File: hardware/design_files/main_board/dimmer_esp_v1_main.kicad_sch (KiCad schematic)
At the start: 53 parts, among them IC1 PEC11S-929K-S0015, J1 SM05B-SRSS-TB_LF__SN_, J4 Conn_01x02, J5 Conn_01x02, J6 Conn_01x02, J7 Conn_01x04, J8 Screw_Terminal_01x03, K1 FTR-LYCA005Y, SW1 Commission, SW2 Reset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

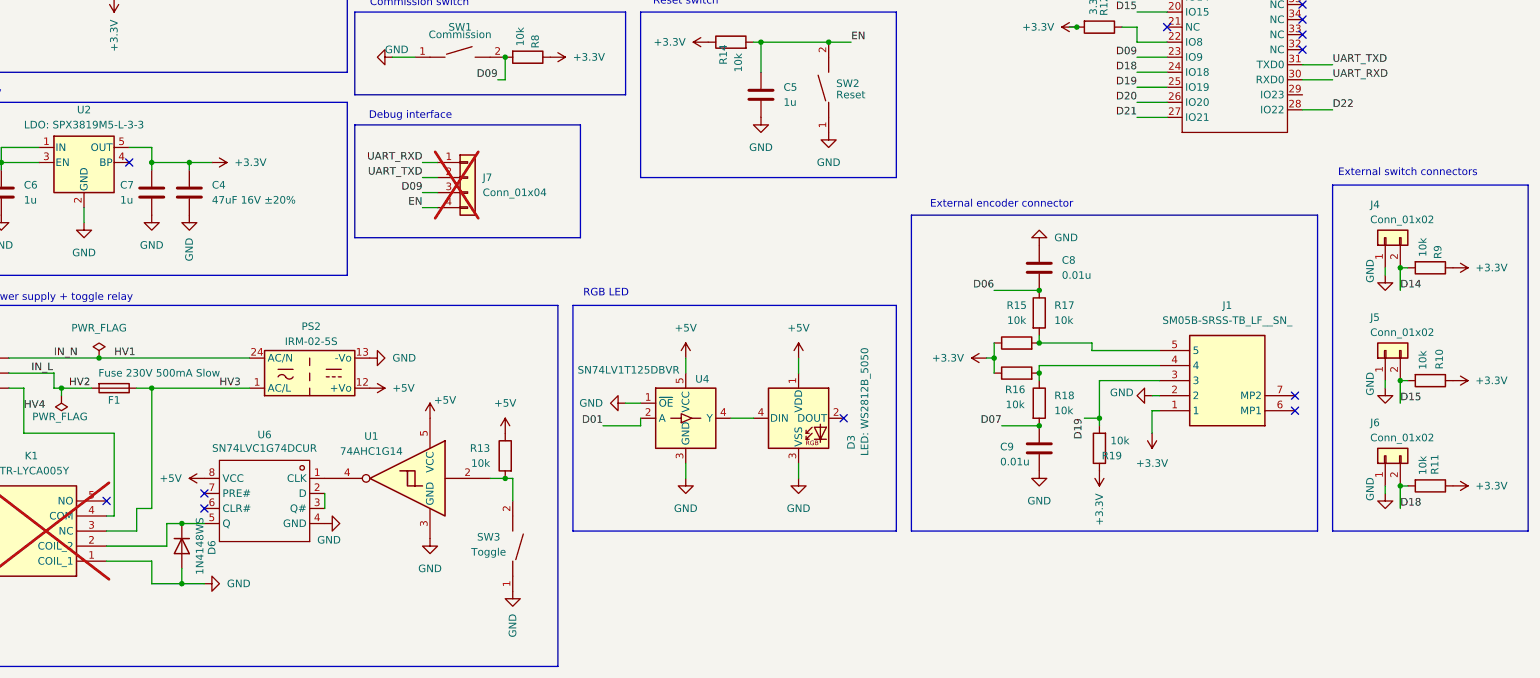
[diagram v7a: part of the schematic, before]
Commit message: Remove debug interface, two JST connectors, replace toggle circuit with using microcontroller
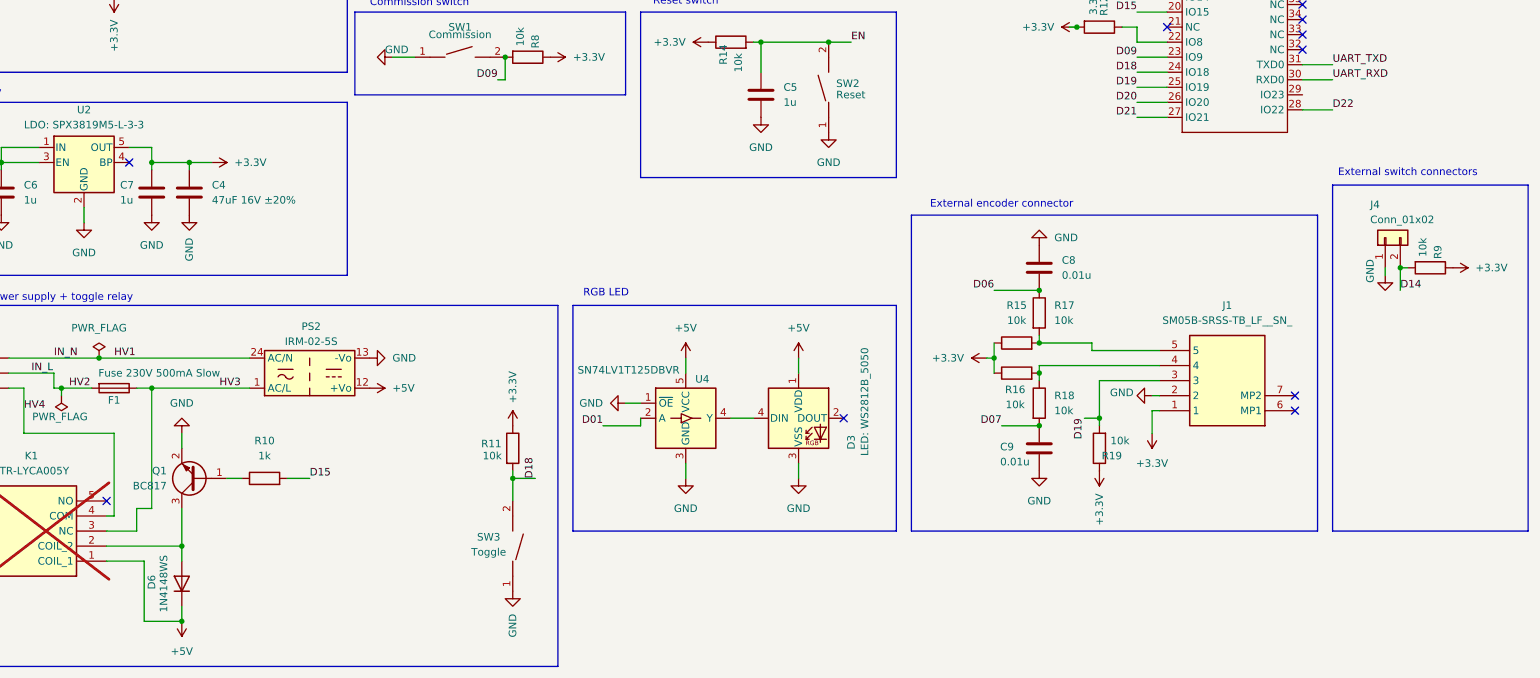
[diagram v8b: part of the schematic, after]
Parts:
- removed J5, J6: Conn_01x02, Connector_JST:JST_SH_SM02B-SRSS-TB_1x02-1MP_P1.00mm_Horizontal, symbol Connector_Generic:Conn_01x02
- removed J7: Conn_01x04, Connector_PinHeader_2.54mm:PinHeader_1x04_P2.54mm_Vertical, symbol Connector_Generic:Conn_01x04
- removed R13: 10k, Resistor_SMD:R_0603_1608Metric, symbol Device:R
- removed U1: 74AHC1G14, Package_TO_SOT_SMD:SOT-353_SC-70-5, symbol 74xGxx:74AHC1G14
- removed U6: SN74LVC1G74DCUR, Package_SO:VSSOP-8_2.3x2mm_P0.5mm, symbol 74xx:SN74LVC1G74DCUR_C70285
- added Q1: BC817, Package_TO_SOT_SMD:SOT-23, symbol Transistor_BJT:BC817
- R10: value 10k -> 1k; footprint Resistor_SMD:R_0603_1608Metric -> (none); LCSC C25804 -> (none)
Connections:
- net +3.3V: no longer R10.1
- net +5V: now also D6.1 (K), K1.1 (COIL_1)
- net D18: now also SW3.2
- net GND: now also Q1.2 (E); no longer D6.2 (A), K1.1 (COIL_1)
- net at K1.2 (COIL_2): now also D6.2 (A), Q1.3 (C); no longer D6.1 (K)
- new net: Q1.1 (B), R10.1
- no-connect marks 26 -> 24
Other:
- note removed: "Debug interface"
- moved on the sheet: D6, R11
